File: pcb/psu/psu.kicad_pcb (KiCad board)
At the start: 2 copper layers, 44.4 x 33 mm, 3 parts, among them J1 VIN, J2 HEADER-1x04, J3 HEADER-1x01

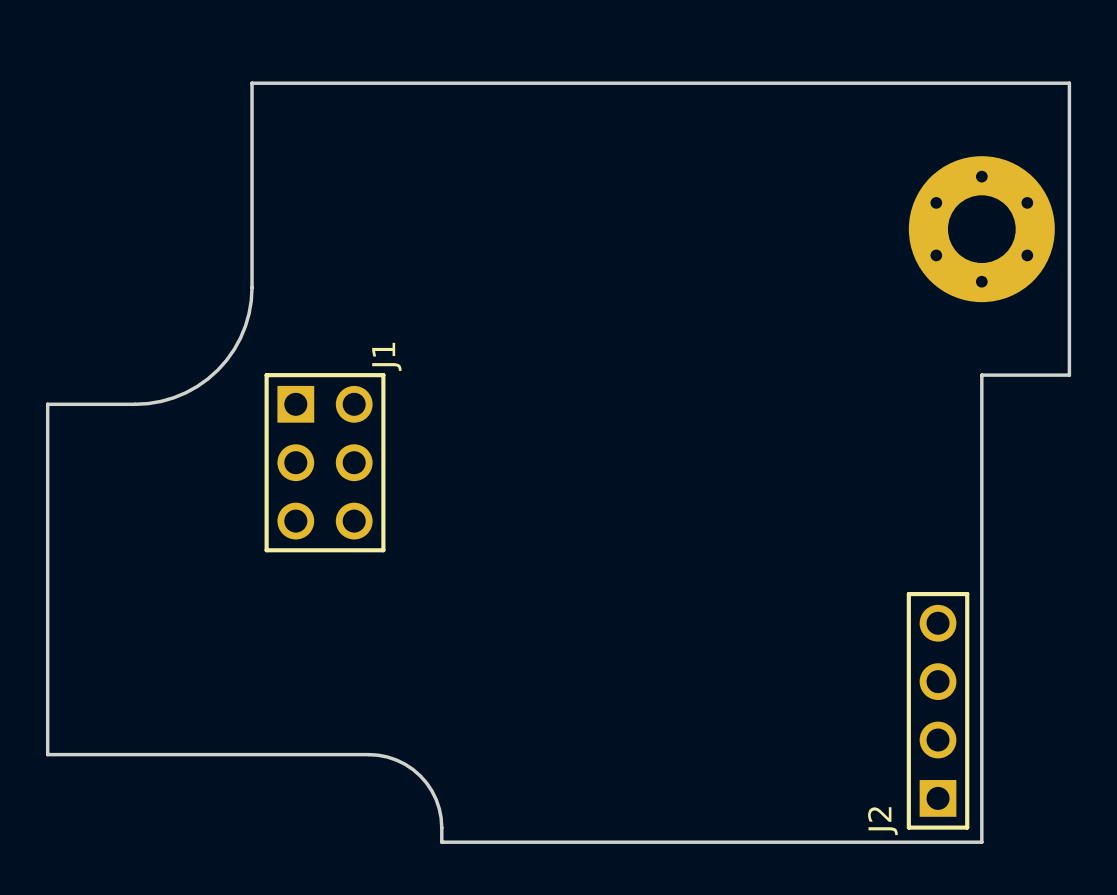
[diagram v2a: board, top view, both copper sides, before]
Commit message: Corrected solder mask clearance
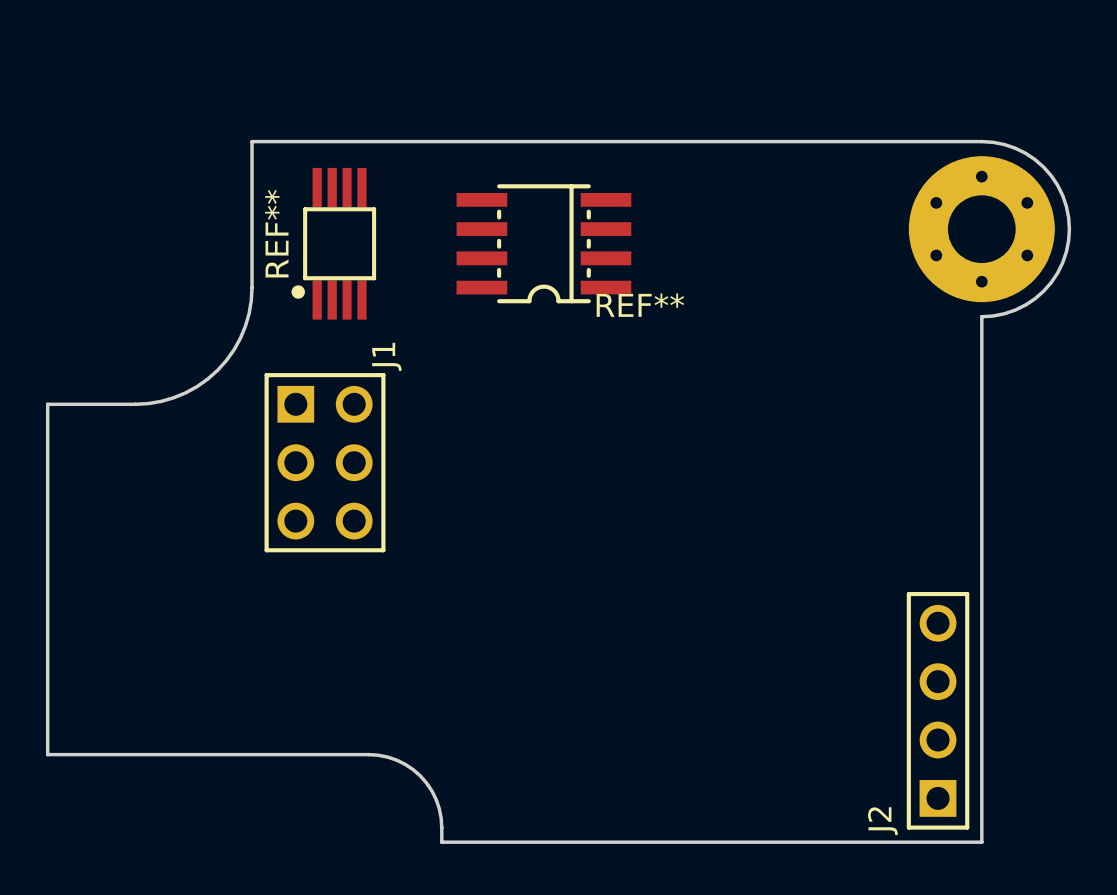
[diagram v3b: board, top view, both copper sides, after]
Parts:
- added REF**: VAL**, smt-sop:MSOP8, F.Cu at (145.4, 94.6)
- added REF**: VAL**, smt-soic:SOIC8, F.Cu at (154.3, 94.6)
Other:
- board size 44.4 x 33 mm -> 44.4 x 30.5 mm
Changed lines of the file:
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@@
   (general
     (thickness 1.6)
-    (drawings 12)
+    (drawings 11)
     (tracks 0)
     (zones 0)
-    (modules 3)
+    (modules 5)
     (nets 9)
   )
@@
       (clearance 0.635) (zone_connect 2))
   )
-  (gr_line (start 177.165 100.33) (end 177.165 87.63) (layer Edge.Cuts) (width 0.15))
-  (gr_line (start 173.355 100.33) (end 177.165 100.33) (layer Edge.Cuts) (width 0.15))
+  (module smt-sop:MSOP8 (layer F.Cu)
+    (at 145.415 94.615)
+    (descr "MSOP - 8 Pins (JEDEC MO-187)")
+    (clearance 0.254)
+    (fp_text reference REF** (at -2.1 1.6 90) (layer F.SilkS)
+      (effects (font (size 1 1) (thickness 0.18)) (justify left bottom))
+    )
+    (fp_text value VAL** (at 2.9 0 90) (layer F.SilkS) hide
+      (effects (font (size 1 1) (thickness 0.18)))
+    )
+    (fp_line (start -1.5 -1.5) (end -1.5 1.5) (layer F.SilkS) (width 0.1778))
+    (fp_line (start 1.5 -1.5) (end -1.5 -1.5) (layer F.SilkS) (width 0.1778))
+    (fp_line (start 1.5 1.5) (end 1.5 -1.5) (layer F.SilkS) (width 0.1778))
+    (fp_line (start -1.5 1.5) (end 1.5 1.5) (layer F.SilkS) (width 0.1778))
+    (fp_circle (center -1.8 2.1) (end -1.7 2.2) (layer F.SilkS) (width 0.3))
+    (fp_line (start -1.8 -3.6) (end 1.8 -3.6) (layer F.CrtYd) (width 0.05))
+    (fp_line (start 1.8 -3.6) (end 1.8 3.6) (layer F.CrtYd) (width 0.05))
+    (fp_line (start 1.8 3.6) (end -1.8 3.6) (layer F.CrtYd) (width 0.05))
+    (fp_line (start -1.8 3.6) (end -1.8 -3.6) (layer F.CrtYd) (width 0.05))
+    (pad 4 smd rect (at 0.975 2.45 270) (size 1.7 0.4) (layers F.Cu F.Paste F.Mask)
+      (solder_mask_margin 0.08) (clearance 0.25))
+    (pad 3 smd rect (at 0.325 2.45 270) (size 1.7 0.4) (layers F.Cu F.Paste F.Mask)
+      (solder_mask_margin 0.08) (clearance 0.25))
+    (pad 2 smd rect (at -0.325 2.45 270) (size 1.7 0.4) (layers F.Cu F.Paste F.Mask)
+      (solder_mask_margin 0.08) (clearance 0.25))
+    (pad 1 smd rect (at -0.975 2.45 270) (size 1.7 0.4) (layers F.Cu F.Paste F.Mask)
+      (solder_mask_margin 0.08) (clearance 0.25))
+    (pad 8 smd rect (at -0.975 -2.45 270) (size 1.7 0.4) (layers F.Cu F.Paste F.Mask)
+      (solder_mask_margin 0.08) (clearance 0.25))
+    (pad 5 smd rect (at 0.975 -2.45 270) (size 1.7 0.4) (layers F.Cu F.Paste F.Mask)
+      (solder_mask_margin 0.08) (clearance 0.25))
+    (pad 6 smd rect (at 0.325 -2.45 270) (size 1.7 0.4) (layers F.Cu F.Paste F.Mask)
+      (solder_mask_margin 0.08) (clearance 0.25))
+    (pad 7 smd rect (at -0.325 -2.45 270) (size 1.7 0.4) (layers F.Cu F.Paste F.Mask)
+      (solder_mask_margin 0.08) (clearance 0.25))
+    (model smt-sop.pretty/MSOP8.wrl
+      (at (xyz 0 0 0))
+      (scale (xyz 1 1 1))
+      (rotate (xyz 0 0 0))
+    )
+  )
+  (module smt-soic:SOIC8 (layer F.Cu)
+    (at 154.305 94.615 90)
+    (descr "SOIC - 8 Pins (JEDEC MS-012AA)")
+    (tags SOIC)
+    (fp_text reference REF** (at -3.302 2.159 180) (layer F.SilkS)
+      (effects (font (size 1 1) (thickness 0.18)) (justify left bottom))
+    )
+    (fp_text value VAL** (at 3.937 0 180) (layer F.SilkS) hide
+      (effects (font (size 1 1) (thickness 0.18)))
+    )
+    (fp_arc (start -2.5 0) (end -2.5 -0.635) (angle 180) (layer F.SilkS) (width 0.18))
+    (fp_line (start 1.143 1.95) (end 1.397 1.95) (layer F.SilkS) (width 0.18))
+    (fp_line (start -0.127 1.95) (end 0.127 1.95) (layer F.SilkS) (width 0.18))
+    (fp_line (start -1.397 1.95) (end -1.143 1.95) (layer F.SilkS) (width 0.18))
+    (fp_line (start 1.143 -1.95) (end 1.397 -1.95) (layer F.SilkS) (width 0.18))
+    (fp_line (start -0.127 -1.95) (end 0.127 -1.95) (layer F.SilkS) (width 0.18))
+    (fp_line (start -1.397 -1.95) (end -1.143 -1.95) (layer F.SilkS) (width 0.18))
+    (fp_line (start 2.5 1.2) (end -2.5 1.2) (layer F.SilkS) (width 0.18))
+    (fp_line (start -2.5 -0.635) (end -2.5 -1.95) (layer F.SilkS) (width 0.18))
+    (fp_line (start -2.5 1.95) (end -2.5 0.635) (layer F.SilkS) (width 0.18))
+    (fp_line (start 2.5 -1.95) (end 2.5 1.95) (layer F.SilkS) (width 0.18))
+    (fp_line (start -2.8 4.1) (end -2.8 -4.1) (layer F.CrtYd) (width 0.05))
+    (fp_line (start 2.8 4.1) (end -2.8 4.1) (layer F.CrtYd) (width 0.05))
+    (fp_line (start 2.8 -4.1) (end 2.8 4.1) (layer F.CrtYd) (width 0.05))
+    (fp_line (start -2.8 -4.1) (end 2.8 -4.1) (layer F.CrtYd) (width 0.05))
+    (pad 5 smd rect (at 1.905 -2.7 90) (size 0.6 2.2) (layers F.Cu F.Paste F.Mask))
+    (pad 6 smd rect (at 0.635 -2.7 90) (size 0.6 2.2) (layers F.Cu F.Paste F.Mask))
+    (pad 8 smd rect (at -1.905 -2.7 90) (size 0.6 2.2) (layers F.Cu F.Paste F.Mask))
+    (pad 4 smd rect (at 1.905 2.7 90) (size 0.6 2.2) (layers F.Cu F.Paste F.Mask))
+    (pad 3 smd rect (at 0.635 2.7 90) (size 0.6 2.2) (layers F.Cu F.Paste F.Mask))
+    (pad 1 smd rect (at -1.905 2.7 90) (size 0.6 2.2) (layers F.Cu F.Paste F.Mask))
+    (pad 7 smd rect (at -0.635 -2.7 90) (size 0.6 2.2) (layers F.Cu F.Paste F.Mask))
+    (pad 2 smd rect (at -0.635 2.7 90) (size 0.6 2.2) (layers F.Cu F.Paste F.Mask))
+    (model smt-soic.pretty/8.wrl
+      (at (xyz 0 0 0))
+      (scale (xyz 1 1 1))
+      (rotate (xyz 0 0 -90))
+    )
+  )
+  (gr_arc (start 173.355 93.98) (end 173.355 97.79) (angle -180) (layer Edge.Cuts) (width 0.15))
   (gr_arc (start 146.685 120.015) (end 149.86 120.015) (angle -90) (layer Edge.Cuts) (width 0.15))
   (gr_line (start 132.715 101.6) (end 132.715 116.84) (layer Edge.Cuts) (width 0.15))
   (gr_line (start 136.525 101.6) (end 132.715 101.6) (layer Edge.Cuts) (width 0.15))
   (gr_arc (start 136.525 96.52) (end 136.525 101.6) (angle -90) (layer Edge.Cuts) (width 0.15))
-  (gr_line (start 141.605 87.63) (end 141.605 96.52) (layer Edge.Cuts) (width 0.15))
-  (gr_line (start 177.165 87.63) (end 141.605 87.63) (layer Edge.Cuts) (width 0.15))
-  (gr_line (start 173.355 120.65) (end 173.355 100.33) (layer Edge.Cuts) (width 0.15))
+  (gr_line (start 141.605 90.17) (end 141.605 96.52) (layer Edge.Cuts) (width 0.15))
+  (gr_line (start 173.355 90.17) (end 141.605 90.17) (layer Edge.Cuts) (width 0.15))
+  (gr_line (start 173.355 120.65) (end 173.355 97.79) (layer Edge.Cuts) (width 0.15))
   (gr_line (start 149.86 120.65) (end 173.355 120.65) (layer Edge.Cuts) (width 0.15))
   (gr_line (start 149.86 120.015) (end 149.86 120.65) (layer Edge.Cuts) (width 0.15))

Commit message: Changed pin for VUSB detection on U3
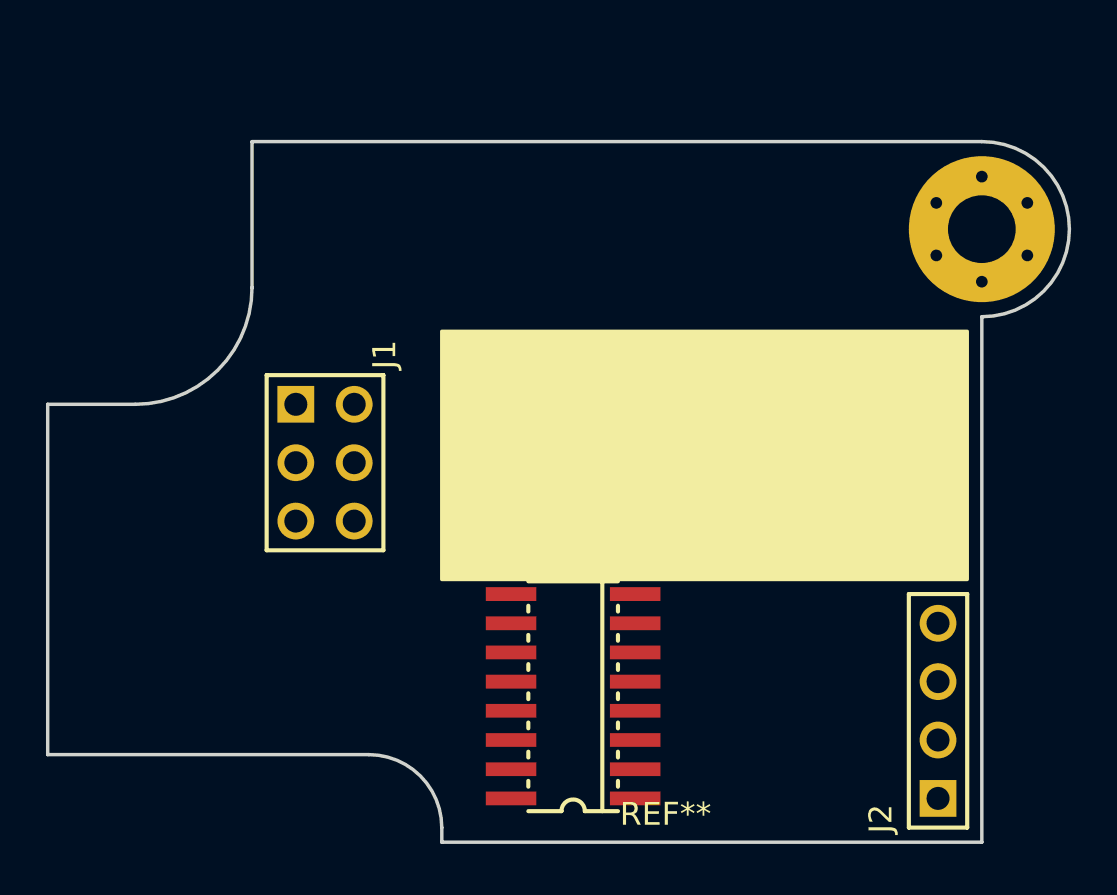
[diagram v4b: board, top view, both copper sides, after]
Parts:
- removed the REF** at (145.4, 94.6)
- removed the REF** at (154.3, 94.6)
- added REF**: VAL**, smt-soic:SOIC16N, F.Cu at (155.6, 114.3)
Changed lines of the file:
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@@
   (general
     (thickness 1.6)
-    (drawings 11)
+    (drawings 12)
     (tracks 0)
     (zones 0)
-    (modules 5)
+    (modules 4)
     (nets 9)
   )
@@
       (clearance 0.635) (zone_connect 2))
   )
-  (module smt-sop:MSOP8 (layer F.Cu)
-    (at 145.415 94.615)
-    (descr "MSOP - 8 Pins (JEDEC MO-187)")
-    (clearance 0.254)
-    (fp_text reference REF** (at -2.1 1.6 90) (layer F.SilkS)
+  (module smt-soic:SOIC16N (layer F.Cu)
+    (at 155.575 114.3 90)
+    (descr "SOIC - 16 pins - Narrow (JEDEC MS-012-AA)")
+    (tags SOIC)
+    (fp_text reference REF** (at -5.715 2.032 180) (layer F.SilkS)
       (effects (font (size 1 1) (thickness 0.18)) (justify left bottom))
     )
-    (fp_text value VAL** (at 2.9 0 90) (layer F.SilkS) hide
-      (effects (font (size 1 1) (thickness 0.18)))
-    )
-    (fp_line (start -1.5 -1.5) (end -1.5 1.5) (layer F.SilkS) (width 0.1778))
-    (fp_line (start 1.5 -1.5) (end -1.5 -1.5) (layer F.SilkS) (width 0.1778))
-    (fp_line (start 1.5 1.5) (end 1.5 -1.5) (layer F.SilkS) (width 0.1778))
-    (fp_line (start -1.5 1.5) (end 1.5 1.5) (layer F.SilkS) (width 0.1778))
-    (fp_circle (center -1.8 2.1) (end -1.7 2.2) (layer F.SilkS) (width 0.3))
-    (fp_line (start -1.8 -3.6) (end 1.8 -3.6) (layer F.CrtYd) (width 0.05))
-    (fp_line (start 1.8 -3.6) (end 1.8 3.6) (layer F.CrtYd) (width 0.05))
-    (fp_line (start 1.8 3.6) (end -1.8 3.6) (layer F.CrtYd) (width 0.05))
-    (fp_line (start -1.8 3.6) (end -1.8 -3.6) (layer F.CrtYd) (width 0.05))
-    (pad 4 smd rect (at 0.975 2.45 270) (size 1.7 0.4) (layers F.Cu F.Paste F.Mask)
-      (solder_mask_margin 0.08) (clearance 0.25))
-    (pad 3 smd rect (at 0.325 2.45 270) (size 1.7 0.4) (layers F.Cu F.Paste F.Mask)
-      (solder_mask_margin 0.08) (clearance 0.25))
-    (pad 2 smd rect (at -0.325 2.45 270) (size 1.7 0.4) (layers F.Cu F.Paste F.Mask)
-      (solder_mask_margin 0.08) (clearance 0.25))
-    (pad 1 smd rect (at -0.975 2.45 270) (size 1.7 0.4) (layers F.Cu F.Paste F.Mask)
-      (solder_mask_margin 0.08) (clearance 0.25))
-    (pad 8 smd rect (at -0.975 -2.45 270) (size 1.7 0.4) (layers F.Cu F.Paste F.Mask)
-      (solder_mask_margin 0.08) (clearance 0.25))
-    (pad 5 smd rect (at 0.975 -2.45 270) (size 1.7 0.4) (layers F.Cu F.Paste F.Mask)
-      (solder_mask_margin 0.08) (clearance 0.25))
-    (pad 6 smd rect (at 0.325 -2.45 270) (size 1.7 0.4) (layers F.Cu F.Paste F.Mask)
-      (solder_mask_margin 0.08) (clearance 0.25))
-    (pad 7 smd rect (at -0.325 -2.45 270) (size 1.7 0.4) (layers F.Cu F.Paste F.Mask)
-      (solder_mask_margin 0.08) (clearance 0.25))
-    (model smt-sop.pretty/MSOP8.wrl
-      (at (xyz 0 0 0))
-      (scale (xyz 1 1 1))
-      (rotate (xyz 0 0 0))
-    )
-  )
-  (module smt-soic:SOIC8 (layer F.Cu)
-    (at 154.305 94.615 90)
-    (descr "SOIC - 8 Pins (JEDEC MS-012AA)")
-    (tags SOIC)
-    (fp_text reference REF** (at -3.302 2.159 180) (layer F.SilkS)
-      (effects (font (size 1 1) (thickness 0.18)) (justify left bottom))
-    )
-    (fp_text value VAL** (at 3.937 0 180) (layer F.SilkS) hide
-      (effects (font (size 1 1) (thickness 0.18)))
-    )
-    (fp_arc (start -2.5 0) (end -2.5 -0.635) (angle 180) (layer F.SilkS) (width 0.18))
+    (fp_text value VAL** (at 6.604 0 180) (layer F.SilkS) hide
+      (effects (font (size 1 1) (thickness 0.18)))
+    )
+    (fp_line (start -5 1.27) (end 5 1.27) (layer F.SilkS) (width 0.18))
+    (fp_line (start 3.683 1.95) (end 3.937 1.95) (layer F.SilkS) (width 0.18))
+    (fp_line (start 2.413 1.95) (end 2.667 1.95) (layer F.SilkS) (width 0.18))
     (fp_line (start 1.143 1.95) (end 1.397 1.95) (layer F.SilkS) (width 0.18))
     (fp_line (start -0.127 1.95) (end 0.127 1.95) (layer F.SilkS) (width 0.18))
     (fp_line (start -1.397 1.95) (end -1.143 1.95) (layer F.SilkS) (width 0.18))
+    (fp_line (start -2.667 1.95) (end -2.413 1.95) (layer F.SilkS) (width 0.18))
+    (fp_line (start -3.937 1.95) (end -3.683 1.95) (layer F.SilkS) (width 0.18))
+    (fp_line (start 3.683 -1.95) (end 3.937 -1.95) (layer F.SilkS) (width 0.18))
+    (fp_line (start 2.413 -1.95) (end 2.667 -1.95) (layer F.SilkS) (width 0.18))
     (fp_line (start 1.143 -1.95) (end 1.397 -1.95) (layer F.SilkS) (width 0.18))
     (fp_line (start -0.127 -1.95) (end 0.127 -1.95) (layer F.SilkS) (width 0.18))
     (fp_line (start -1.397 -1.95) (end -1.143 -1.95) (layer F.SilkS) (width 0.18))
-    (fp_line (start 2.5 1.2) (end -2.5 1.2) (layer F.SilkS) (width 0.18))
-    (fp_line (start -2.5 -0.635) (end -2.5 -1.95) (layer F.SilkS) (width 0.18))
-    (fp_line (start -2.5 1.95) (end -2.5 0.635) (layer F.SilkS) (width 0.18))
-    (fp_line (start 2.5 -1.95) (end 2.5 1.95) (layer F.SilkS) (width 0.18))
-    (fp_line (start -2.8 4.1) (end -2.8 -4.1) (layer F.CrtYd) (width 0.05))
-    (fp_line (start 2.8 4.1) (end -2.8 4.1) (layer F.CrtYd) (width 0.05))
-    (fp_line (start 2.8 -4.1) (end 2.8 4.1) (layer F.CrtYd) (width 0.05))
-    (fp_line (start -2.8 -4.1) (end 2.8 -4.1) (layer F.CrtYd) (width 0.05))
-    (pad 5 smd rect (at 1.905 -2.7 90) (size 0.6 2.2) (layers F.Cu F.Paste F.Mask))
-    (pad 6 smd rect (at 0.635 -2.7 90) (size 0.6 2.2) (layers F.Cu F.Paste F.Mask))
-    (pad 8 smd rect (at -1.905 -2.7 90) (size 0.6 2.2) (layers F.Cu F.Paste F.Mask))
-    (pad 4 smd rect (at 1.905 2.7 90) (size 0.6 2.2) (layers F.Cu F.Paste F.Mask))
-    (pad 3 smd rect (at 0.635 2.7 90) (size 0.6 2.2) (layers F.Cu F.Paste F.Mask))
-    (pad 1 smd rect (at -1.905 2.7 90) (size 0.6 2.2) (layers F.Cu F.Paste F.Mask))
-    (pad 7 smd rect (at -0.635 -2.7 90) (size 0.6 2.2) (layers F.Cu F.Paste F.Mask))
-    (pad 2 smd rect (at -0.635 2.7 90) (size 0.6 2.2) (layers F.Cu F.Paste F.Mask))
-    (model smt-soic.pretty/8.wrl
+    (fp_line (start -2.667 -1.95) (end -2.413 -1.95) (layer F.SilkS) (width 0.18))
+    (fp_line (start -3.937 -1.95) (end -3.683 -1.95) (layer F.SilkS) (width 0.18))
+    (fp_arc (start -5 0) (end -5 -0.508) (angle 180) (layer F.SilkS) (width 0.18))
+    (fp_line (start -5 0.508) (end -5 1.95) (layer F.SilkS) (width 0.18))
+    (fp_line (start -5 -1.95) (end -5 -0.508) (layer F.SilkS) (width 0.18))
+    (fp_line (start 5 1.95) (end 5 -1.95) (layer F.SilkS) (width 0.18))
+    (fp_line (start -5.3 4.1) (end -5.3 -4.1) (layer F.CrtYd) (width 0.05))
+    (fp_line (start 5.3 4.1) (end -5.3 4.1) (layer F.CrtYd) (width 0.05))
+    (fp_line (start 5.3 -4.1) (end 5.3 4.1) (layer F.CrtYd) (width 0.05))
+    (fp_line (start -5.3 -4.1) (end 5.3 -4.1) (layer F.CrtYd) (width 0.05))
+    (pad 9 smd rect (at 4.445 -2.7 90) (size 0.6 2.2) (layers F.Cu F.Paste F.Mask))
+    (pad 8 smd rect (at 4.445 2.7 90) (size 0.6 2.2) (layers F.Cu F.Paste F.Mask))
+    (pad 10 smd rect (at 3.175 -2.7 90) (size 0.6 2.2) (layers F.Cu F.Paste F.Mask))
+    (pad 11 smd rect (at 1.905 -2.7 90) (size 0.6 2.2) (layers F.Cu F.Paste F.Mask))
+    (pad 7 smd rect (at 3.175 2.7 90) (size 0.6 2.2) (layers F.Cu F.Paste F.Mask))
+    (pad 6 smd rect (at 1.905 2.7 90) (size 0.6 2.2) (layers F.Cu F.Paste F.Mask))
+    (pad 12 smd rect (at 0.635 -2.7 90) (size 0.6 2.2) (layers F.Cu F.Paste F.Mask))
+    (pad 5 smd rect (at 0.635 2.7 90) (size 0.6 2.2) (layers F.Cu F.Paste F.Mask))
+    (pad 13 smd rect (at -0.635 -2.7 90) (size 0.6 2.2) (layers F.Cu F.Paste F.Mask))
+    (pad 4 smd rect (at -0.635 2.7 90) (size 0.6 2.2) (layers F.Cu F.Paste F.Mask))
+    (pad 14 smd rect (at -1.905 -2.7 90) (size 0.6 2.2) (layers F.Cu F.Paste F.Mask))
+    (pad 15 smd rect (at -3.175 -2.7 90) (size 0.6 2.2) (layers F.Cu F.Paste F.Mask))
+    (pad 3 smd rect (at -1.905 2.7 90) (size 0.6 2.2) (layers F.Cu F.Paste F.Mask))
+    (pad 2 smd rect (at -3.175 2.7 90) (size 0.6 2.2) (layers F.Cu F.Paste F.Mask))
+    (pad 16 smd rect (at -4.445 -2.7 90) (size 0.6 2.2) (layers F.Cu F.Paste F.Mask))
+    (pad 1 smd rect (at -4.445 2.7 90) (size 0.6 2.2) (layers F.Cu F.Paste F.Mask))
+    (model smt-soic.pretty/16N.wrl
       (at (xyz 0 0 0))
       (scale (xyz 1 1 1))
@@
     )
   )
+  (gr_poly (pts (xy 149.86 98.425) (xy 172.72 98.425) (xy 172.72 109.22) (xy 149.86 109.22)) (layer F.SilkS) (width 0.15))
   (gr_arc (start 173.355 93.98) (end 173.355 97.79) (angle -180) (layer Edge.Cuts) (width 0.15))
   (gr_arc (start 146.685 120.015) (end 149.86 120.015) (angle -90) (layer Edge.Cuts) (width 0.15))
